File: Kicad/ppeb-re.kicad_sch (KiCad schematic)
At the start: 34 parts, among them J1 TI-99_Sideport, J4 USB_A, P1 TI-99_Sideport, Q1 2N7002, Q2 2N7002, Q3 2N7002, SW1 SW_Push, U1 Pico, U2 ESP-PSRAM32, U3 74LVC245, U4 74LVC245, U5 74LVC245, U6 74HC138, U7 ESP-PSRAM32

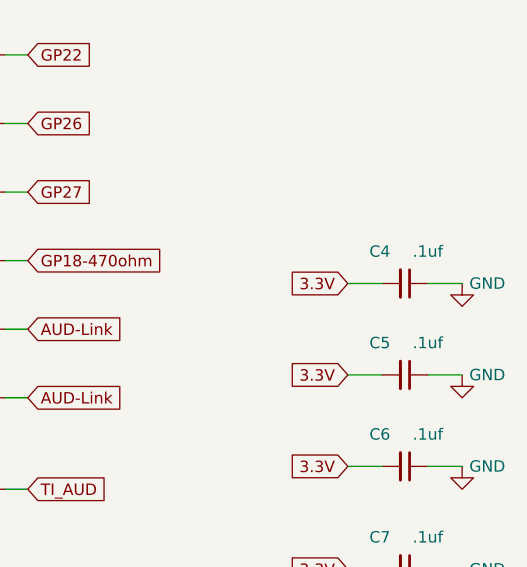
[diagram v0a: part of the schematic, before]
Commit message: Removed C4 - Improved MicroSD Compatibility
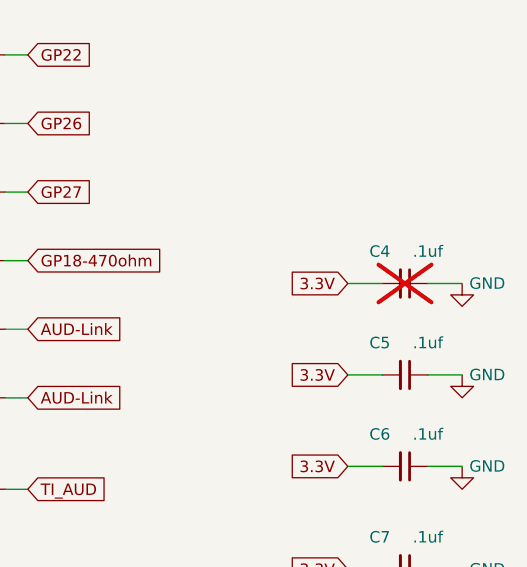
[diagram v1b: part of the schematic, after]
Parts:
- C4: now not fitted; now left out of the parts list
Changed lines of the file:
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@@
 		(unit 1)
 		(exclude_from_sim no)
-		(in_bom yes)
+		(in_bom no)
 		(on_board yes)
-		(dnp no)
+		(dnp yes)
 		(property "Reference" "C4"
 			(at 350.266 142.494 90)

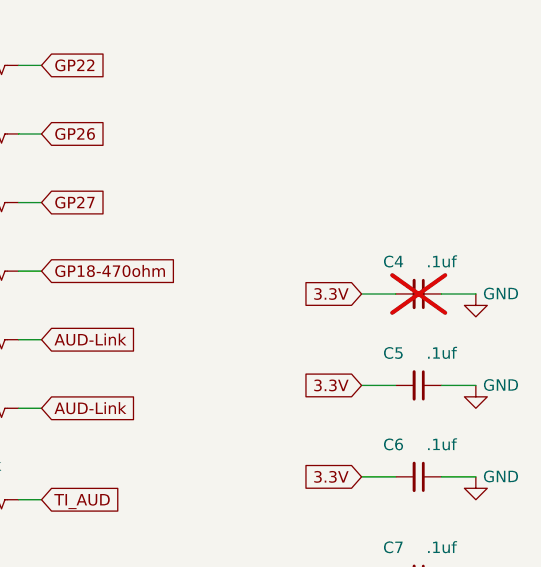
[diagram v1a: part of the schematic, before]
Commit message: Remove c4 from board and schematic
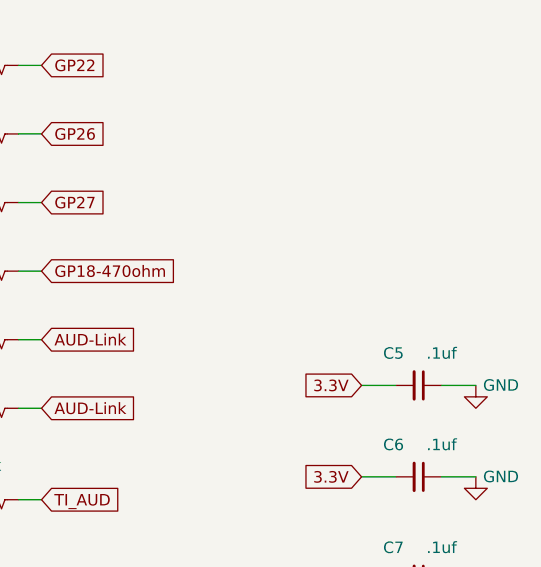
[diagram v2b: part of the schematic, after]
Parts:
- removed C4: .1uf, Capacitor_SMD:C_0805_2012Metric_Pad1.18x1.45mm_HandSolder, symbol Device:C_Small
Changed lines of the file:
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@@
 	(wire
 		(pts
-			(xy 346.71 146.05) (xy 350.52 146.05)
-		)
-		(stroke
-			(width 0)
-			(type default)
-		)
-	)
-	(wire
-		(pts
 			(xy 302.26 212.09) (xy 304.8 212.09)
 		)
@@
 	(wire
 		(pts
-			(xy 355.6 146.05) (xy 359.41 146.05)
-		)
-		(stroke
-			(width 0)
-			(type default)
-		)
-	)
-	(wire
-		(pts
 			(xy 157.48 110.49) (xy 163.83 110.49)
 		)
@@
 		)
 	)
-	(global_label "3.3V"
-		(shape input)
-		(at 346.71 146.05 180)
-		(fields_autoplaced yes)
-		(effects
-			(font
-				(size 1.27 1.27)
-			)
-			(justify right)
-		)
-		(property "Intersheetrefs" "${INTERSHEET_REFS}"
-			(at 340.2666 146.05 0)
-			(effects
-				(font
-					(size 1.27 1.27)
-				)
-				(justify right)
-				(hide yes)
-			)
-		)
-	)
 	(global_label "TI_A4"
 		(shape input)
@@
 	(symbol
 		(lib_id "power:GND")
-		(at 359.41 146.05 0)
-		(unit 1)
-		(exclude_from_sim no)
-		(in_bom yes)
-		(on_board yes)
-		(dnp no)
-		(property "Reference" "#PWR028"
-			(at 359.41 152.4 0)
-			(effects
-				(font
-					(size 1.27 1.27)
-				)
-				(hide yes)
-			)
-		)
-		(property "Value" "GND"
-			(at 362.204 146.05 0)
-			(effects
-				(font
-					(size 1.27 1.27)
-				)
-			)
-		)
-		(property "Footprint" ""
-			(at 359.41 146.05 0)
-			(effects
-				(font
-					(size 1.27 1.27)
-				)
-				(hide yes)
-			)
-		)
-		(property "Datasheet" ""
-			(at 359.41 146.05 0)
-			(effects
-				(font
-					(size 1.27 1.27)
-				)
-				(hide yes)
-			)
-		)
-		(property "Description" ""
-			(at 359.41 146.05 0)
-			(effects
-				(font
-					(size 1.27 1.27)
-				)
-				(hide yes)
-			)
-		)
-		(pin "1"
-		)
-		(instances
-			(project "ppeb-re"
-				(path "/e6371a91-ff23-44d2-b7ef-bd6451c8eb0f"
-					(reference "#PWR028")
-					(unit 1)
-				)
-			)
-		)
-	)
-	(symbol
-		(lib_id "power:GND")
 		(at 358.14 189.23 0)
 		(unit 1)
@@
 					(unit 1)
 				)
-			)
-		)
-	)
-	(symbol
-		(lib_id "Device:C_Small")
-		(at 353.06 146.05 270)
-		(unit 1)
-		(exclude_from_sim no)
-		(in_bom no)
-		(on_board yes)
-		(dnp yes)
-		(property "Reference" "C4"
-			(at 350.266 142.494 90)
-			(effects
-				(font
-					(size 1.27 1.27)
-				)
-			)
-		)
-		(property "Value" ".1uf"
-			(at 355.6 142.494 90)
-			(effects
-				(font
-					(size 1.27 1.27)
-				)
-			)
-		)
-		(property "Footprint" "Capacitor_SMD:C_0805_2012Metric_Pad1.18x1.45mm_HandSolder"
-			(at 353.06 146.05 0)
-			(effects
-				(font
-					(size 1.27 1.27)
-				)
-				(hide yes)
-			)
-		)
-		(property "Datasheet" "~"
-			(at 353.06 146.05 0)
-			(effects
-				(font
-					(size 1.27 1.27)
-				)
-				(hide yes)
-			)
-		)
-		(property "Description" "Unpolarized capacitor, small symbol"
-			(at 353.06 146.05 0)
-			(effects
-				(font
-					(size 1.27 1.27)
-				)
-				(hide yes)
-			)
-		)
-		(property "LCSC Part #" "C38141"
-			(at 353.06 146.05 90)
-			(effects
-				(font
-					(size 1.27 1.27)
-				)
-				(hide yes)
-			)
-		)
-		(pin "1"
-		)
-		(pin "2"
-		)
-		(instances
-			(project "ppeb-re"
-				(path "/e6371a91-ff23-44d2-b7ef-bd6451c8eb0f"
-					(reference "C4")
-					(unit 1)
-				)

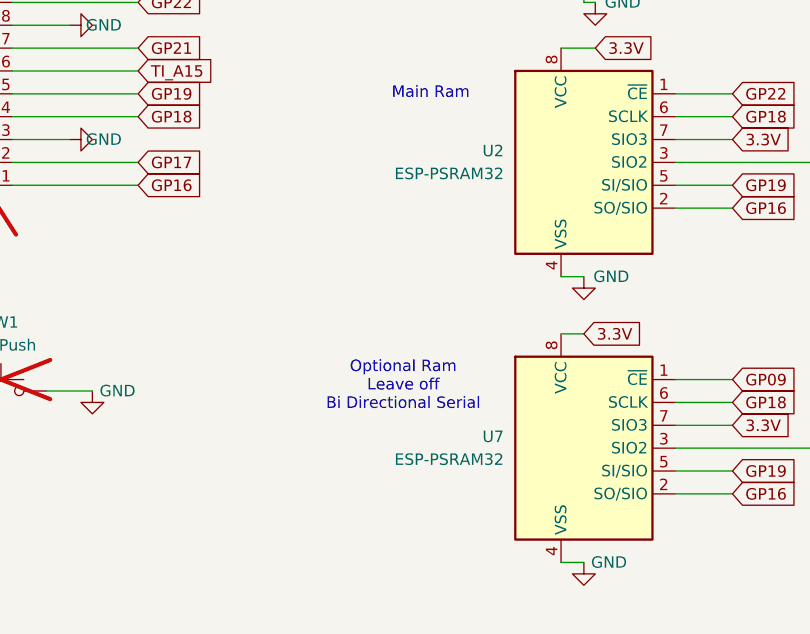
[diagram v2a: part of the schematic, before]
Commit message: Updated PSRam Part Number in schematics and BOM
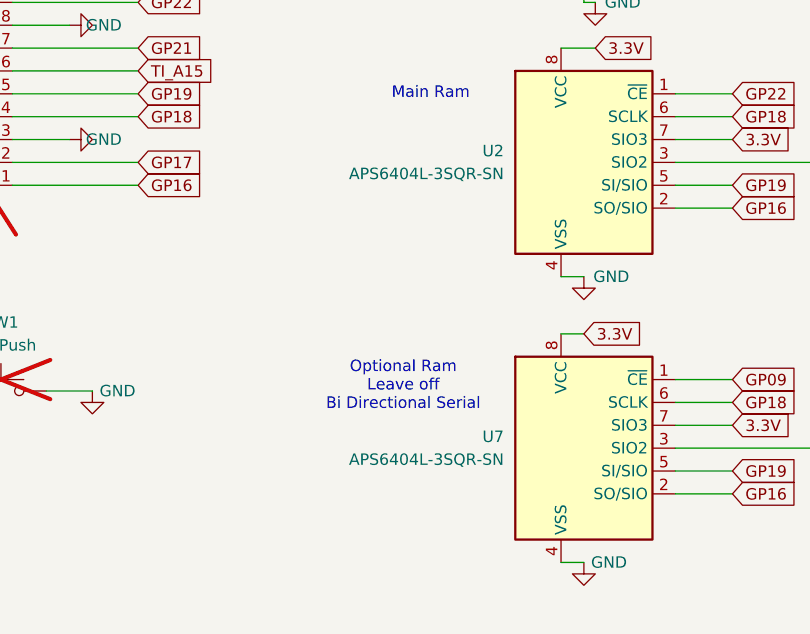
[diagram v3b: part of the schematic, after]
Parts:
- U2, U7: value ESP-PSRAM32 -> APS6404L-3SQR-SN
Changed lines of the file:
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@@
 			)
 		)
-		(property "Value" "ESP-PSRAM32"
+		(property "Value" "APS6404L-3SQR-SN"
 			(at 138.43 87.6299 0)
 			(effects
@@
 			)
 		)
-		(property "Value" "ESP-PSRAM32"
+		(property "Value" "APS6404L-3SQR-SN"
 			(at 138.43 119.3799 0)
 			(effects
